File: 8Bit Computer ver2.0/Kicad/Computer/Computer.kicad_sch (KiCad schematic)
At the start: 0 parts

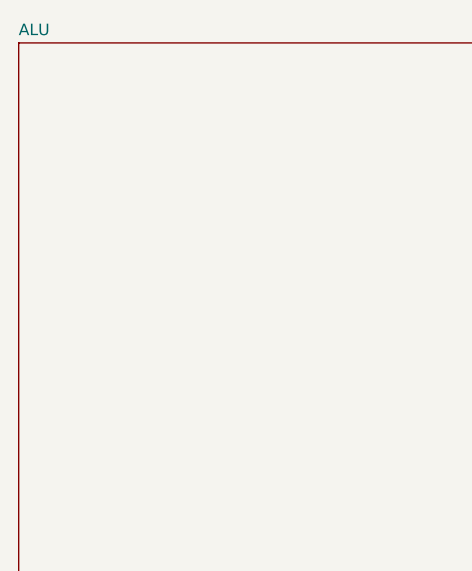
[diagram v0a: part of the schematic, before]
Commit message: parts,Kicad
added 74HCS574 to Kicad
Kicad:
ALU->added Bitwise NOT,OR,XOR,AND
ALU->added A,B 8in OR
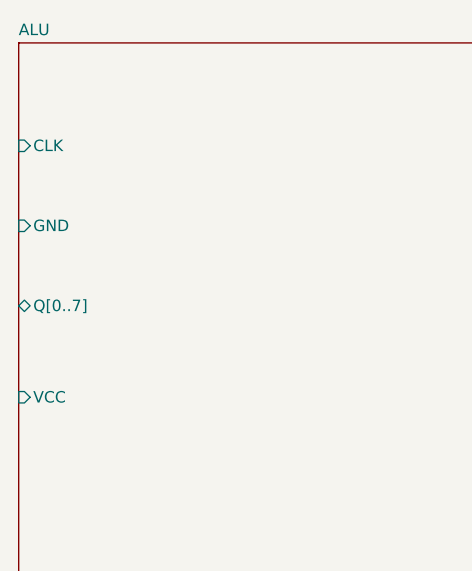
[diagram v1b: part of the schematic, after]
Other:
- sheet ALU ports: added CLK, GND, Q[0..7], VCC; removed none
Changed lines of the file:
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@@
+			)
+		)
+		(pin "CLK" input
+			(at 283.21 96.52 180)
+			(effects
+				(font
+					(size 1.27 1.27)
+				)
+				(justify left)
+			)
+		)
+		(pin "GND" input
+			(at 283.21 105.41 180)
+			(effects
+				(font
+					(size 1.27 1.27)
+				)
+				(justify left)
+			)
+		)
+		(pin "Q[0..7]" tri_state
+			(at 283.21 114.3 180)
+			(effects
+				(font
+					(size 1.27 1.27)
+				)
+				(justify left)
+			)
+		)
+		(pin "VCC" input
+			(at 283.21 124.46 180)
+			(effects
+				(font
+					(size 1.27 1.27)
+				)
+				(justify left)
 			)
 		)

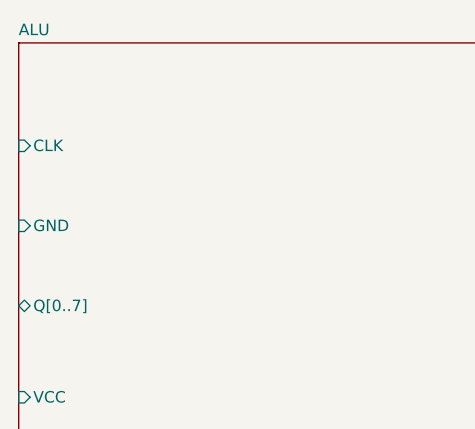
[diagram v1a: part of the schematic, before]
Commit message: Kicad,parts
Kicad:
added FlagRegister
began Inc, Comp
parts:
added comparator for P>Q 682
added faster sram 12ns AS7C
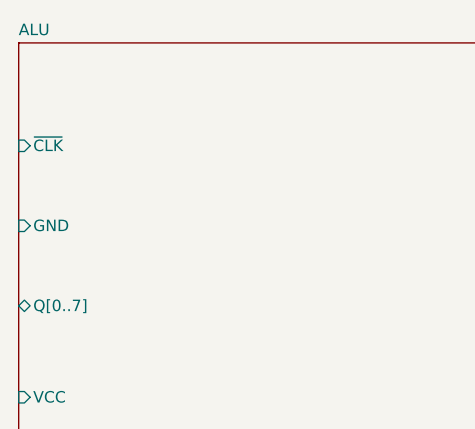
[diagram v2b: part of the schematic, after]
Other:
- sheet ALU ports: added ~{CLK}; removed CLK
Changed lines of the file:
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@@
-			)
-		)
-		(pin "CLK" input
-			(at 283.21 96.52 180)
-			(effects
-				(font
-					(size 1.27 1.27)
-				)
-				(justify left)
 			)
 		)
@@
 			(effects
 				(font
+					(size 1.27 1.27)
+				)
+				(justify left)
+			)
+		)
+		(pin "~{CLK}" input
+			(at 283.21 96.52 180)
+			(effects
+				(font

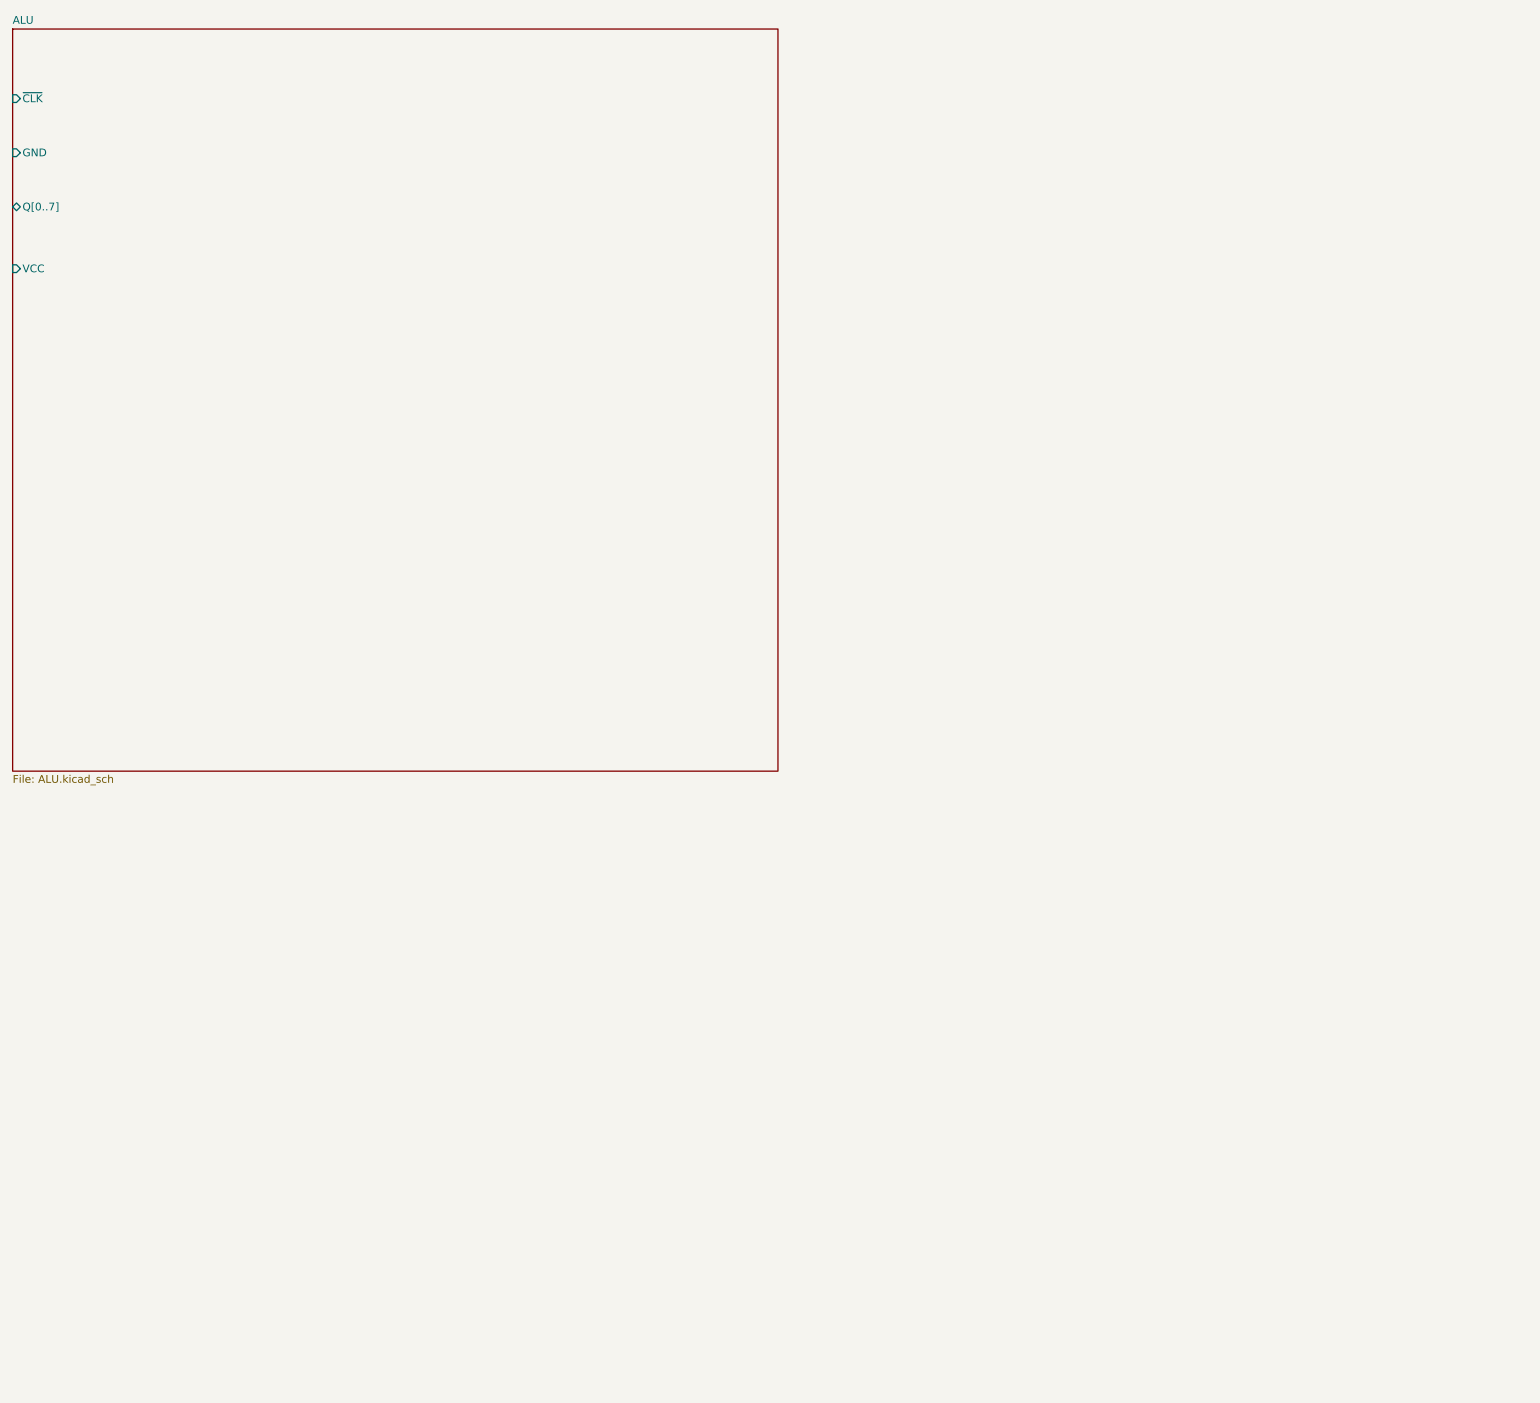
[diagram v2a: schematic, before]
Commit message: parts,Kicad
parts:
changed 8xDlatch HCS to ABT 574
waiting for SRAM CAD Model
Kicad:
imported AHC types of ICs
added ProgrammeCounter
finished Comparator
changed all HCS to AHC except 3in OR ->no AHC Version
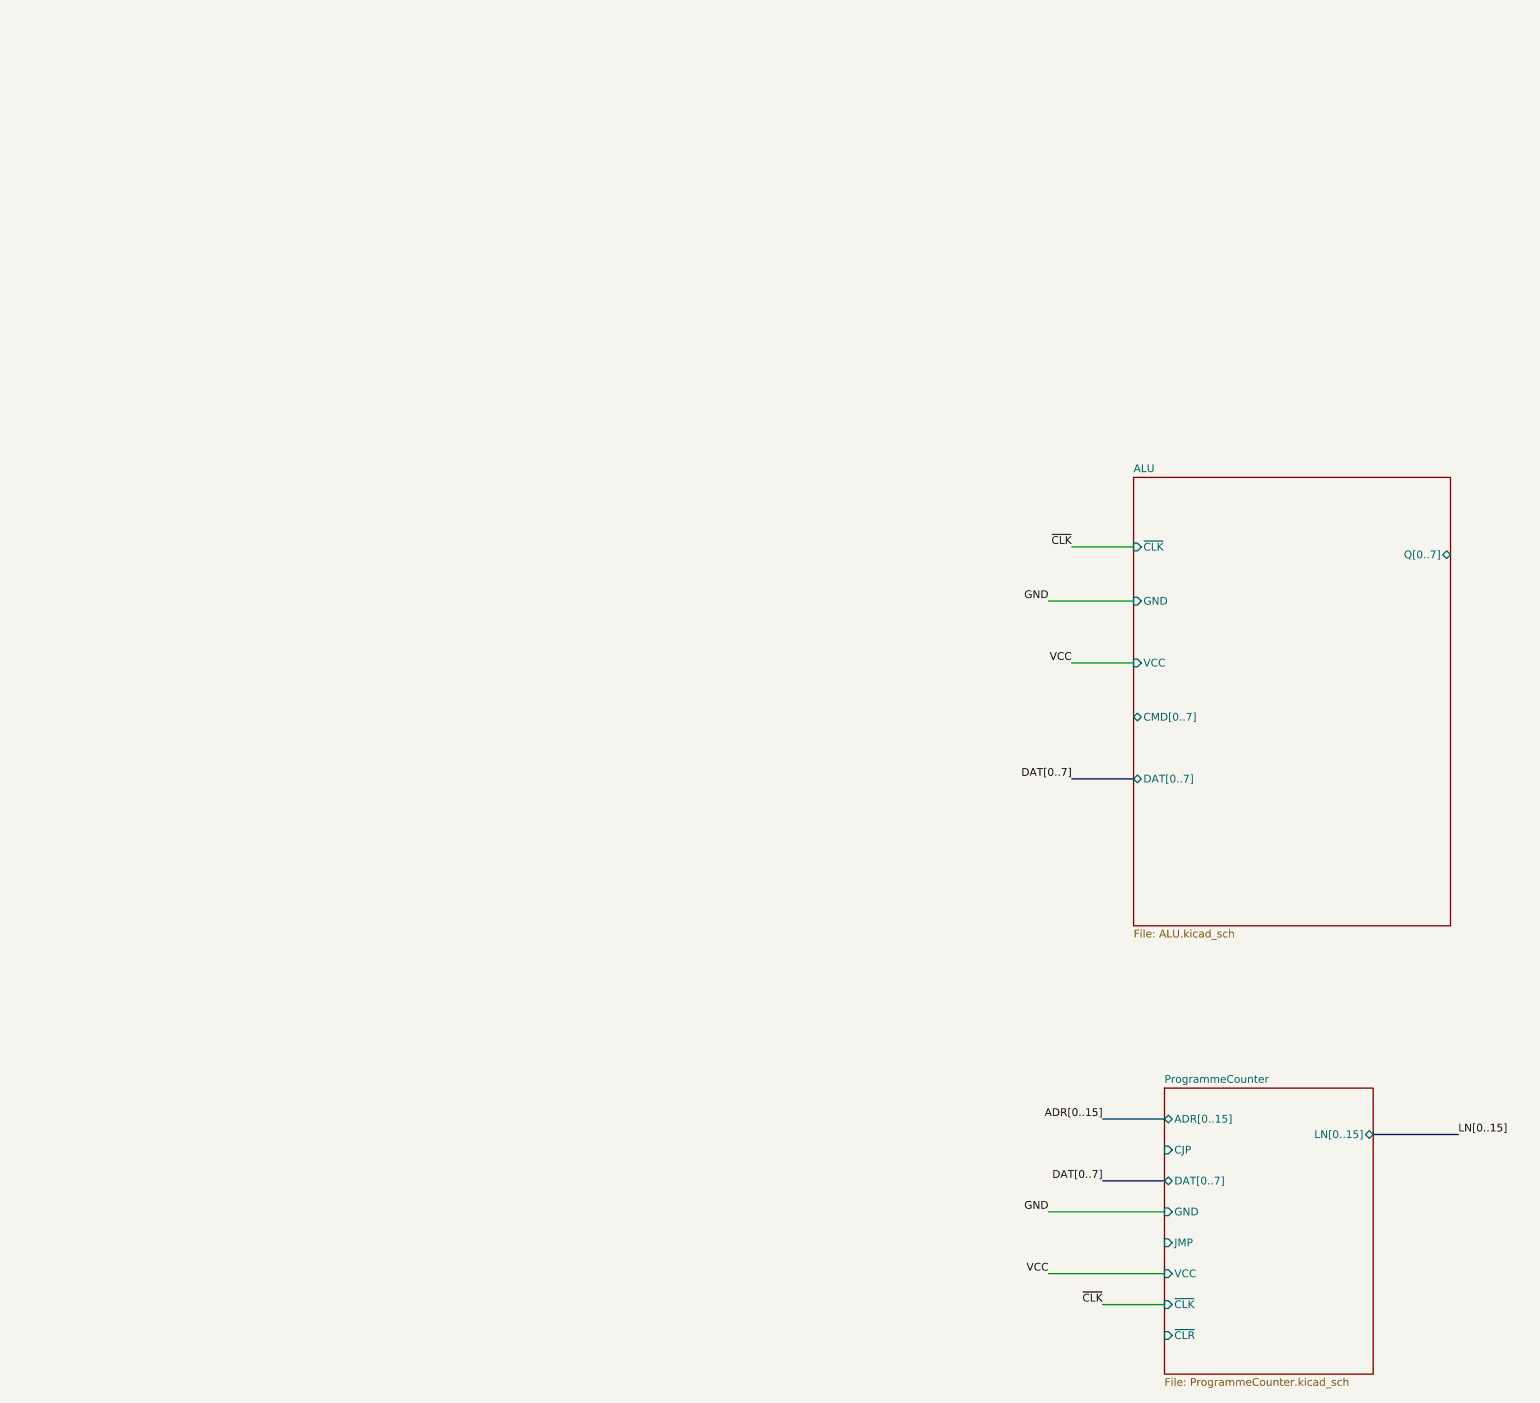
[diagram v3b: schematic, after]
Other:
- added sheet ProgrammeCounter (ProgrammeCounter.kicad_sch)
- sheet ALU ports: added CMD[0..7], DAT[0..7]; removed none

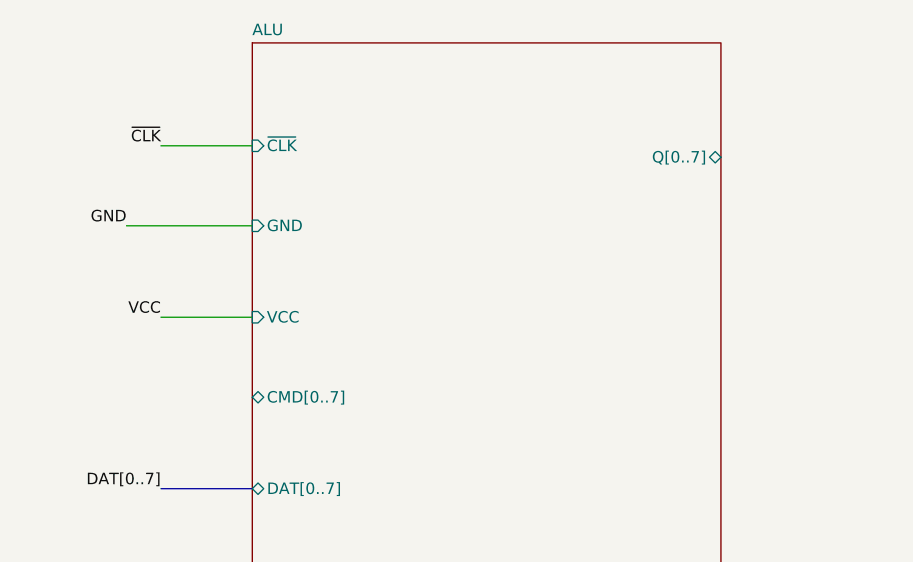
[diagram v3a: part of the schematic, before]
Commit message: Kicad
added Register 2(0x22 u 0x23) and 3(0x13 u 0x14)
added BarrelShiftRegister
added AdderSubstractor
added cmd Comparators to the bitwise and binary Logic
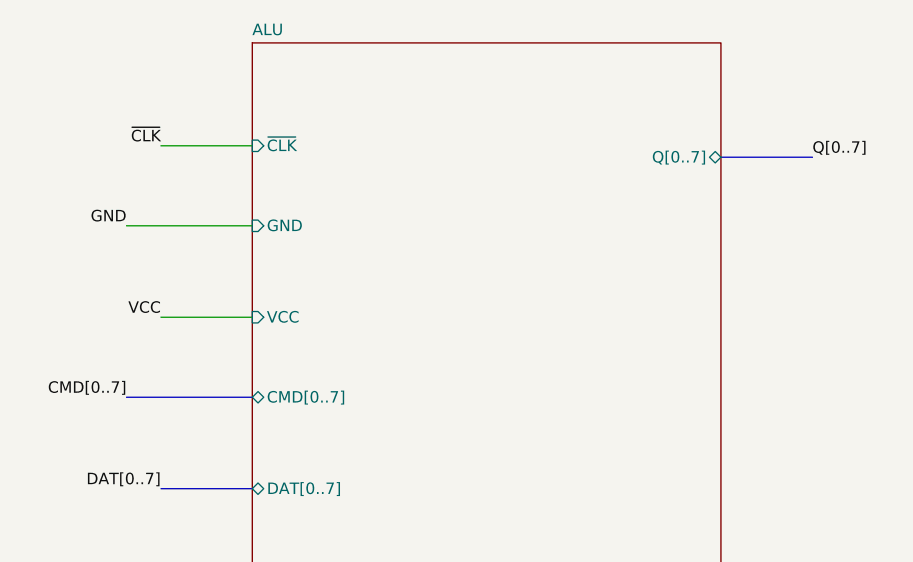
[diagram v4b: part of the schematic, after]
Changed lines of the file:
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@@
+		)
+	)
+	(bus
+		(pts
+			(xy 453.39 198.12) (xy 467.36 198.12)
+		)
+		(stroke
+			(width 0)
+			(type default)
 		)
 	)
@@
 		(pts
 			(xy 457.2 189.23) (xy 467.36 189.23)
+		)
+		(stroke
+			(width 0)
+			(type default)
+		)
+	)
+	(bus
+		(pts
+			(xy 519.43 171.45) (xy 529.59 171.45)
 		)
 		(stroke
@@
 		)
 	)
+	(label "Q[0..7]"
+		(at 529.59 171.45 0)
+		(effects
+			(font
+				(size 1.27 1.27)
+			)
+			(justify left bottom)
+		)
+	)
 	(label "DAT[0..7]"
 		(at 457.2 208.28 180)
@@
 		(effects
 			(font
+				(size 1.27 1.27)
+			)
+			(justify right bottom)
+		)
+	)
+	(label "CMD[0..7]"
+		(at 453.39 198.12 180)
+		(effects
+			(font
